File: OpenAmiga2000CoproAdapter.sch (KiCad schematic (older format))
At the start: 17 parts, among them CN1 A2000_COPRO_SLOT, P1 CONN_2, P10 CONN_1, P11 CONN_1, P12 CONN_1, P13 CONN_1, P14 CONN_1, P15 CONN_1, P2 CONN_2, P3 CONN_2, P4 CONN_2, P5 CONN_1, P6 CONN_1, P7 CONN_1, P8 CONN_1, P9 CONN_1, U1 68000D

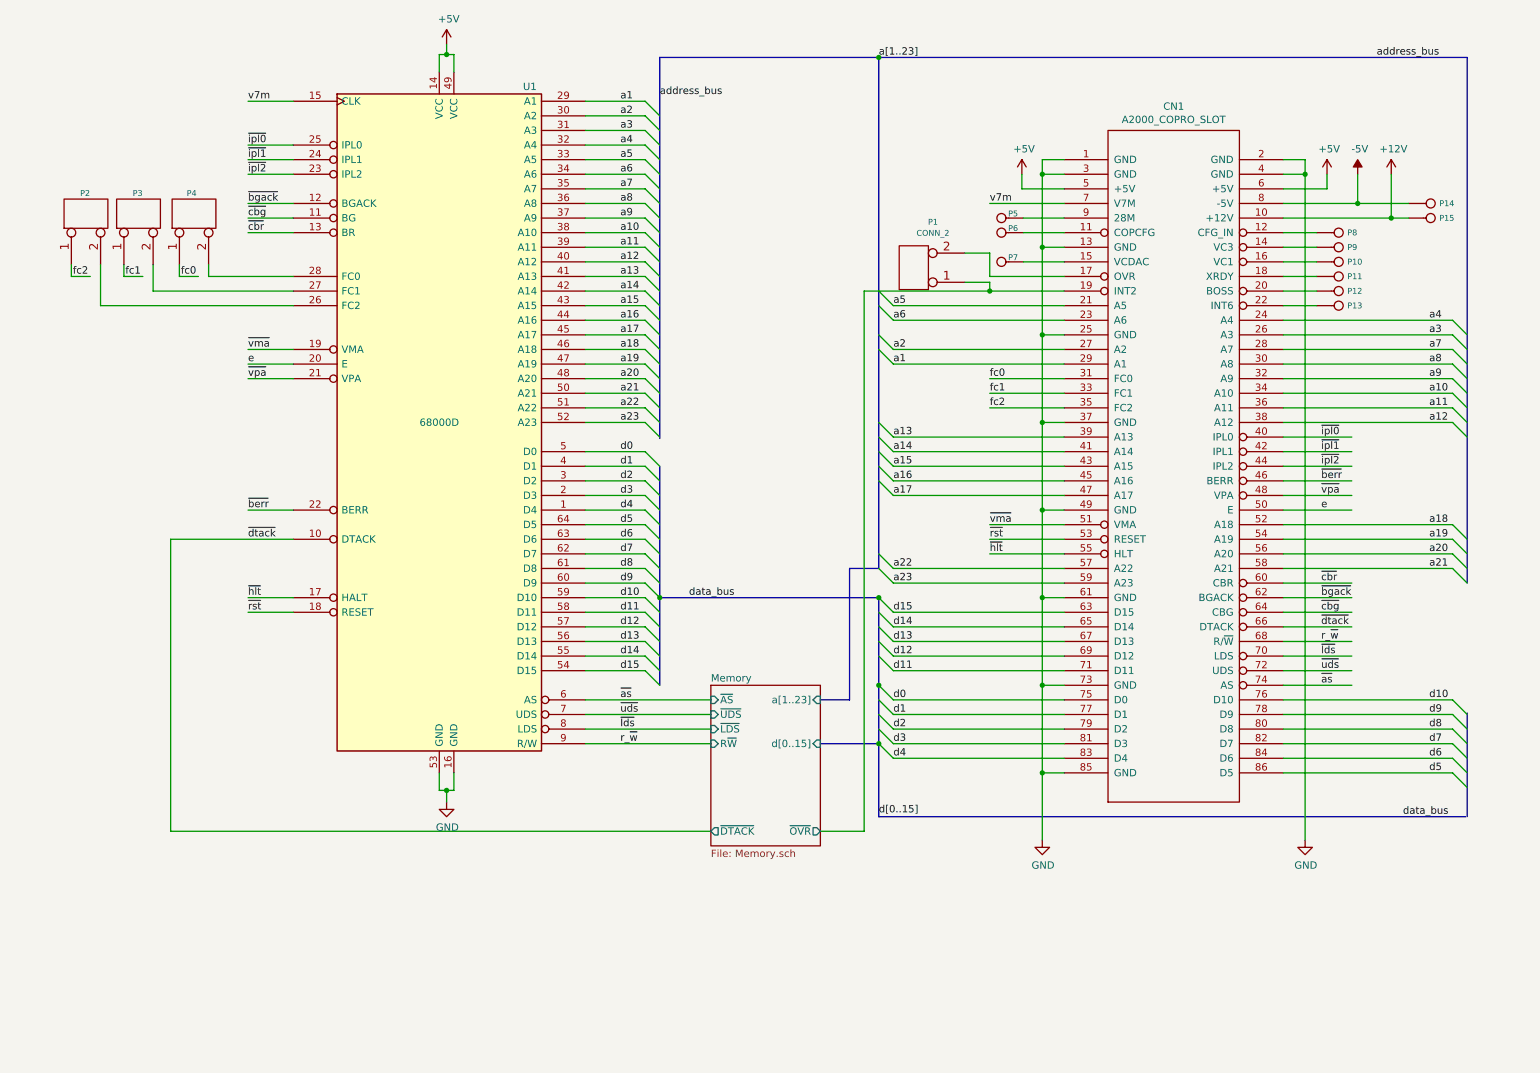
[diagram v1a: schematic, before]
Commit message: finish turbo section
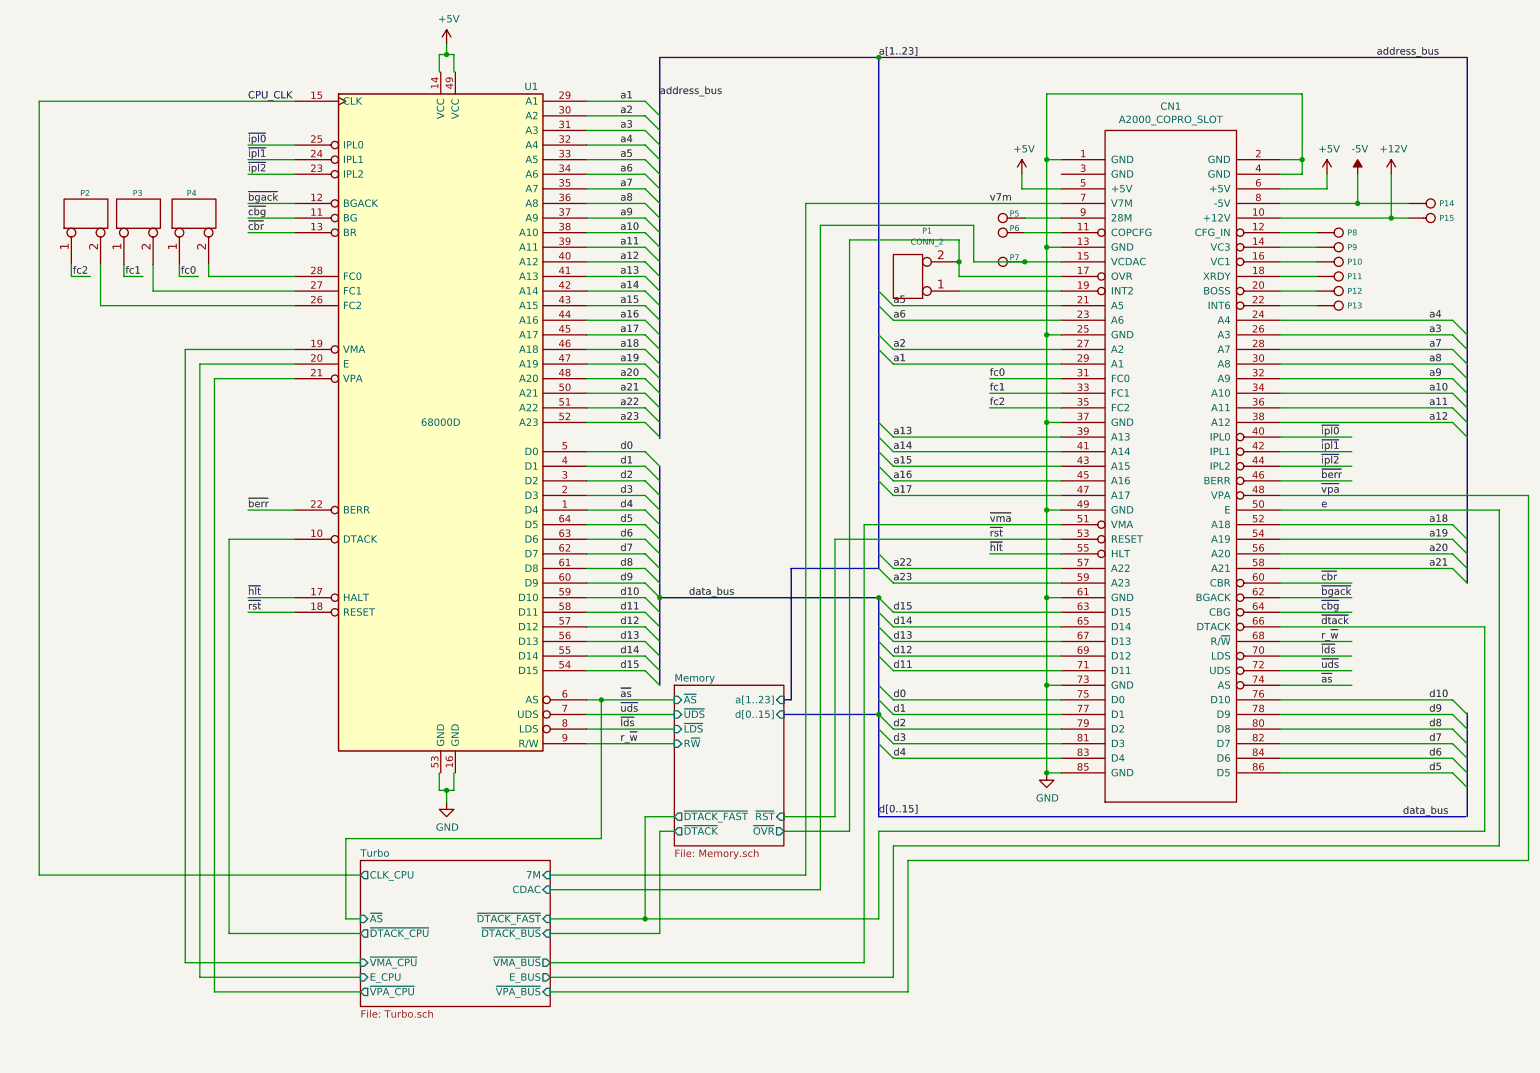
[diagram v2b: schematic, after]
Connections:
- net labels added: CPU_CLK
- wire segments 191 -> 230
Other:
- moved on the sheet: CN1, P1

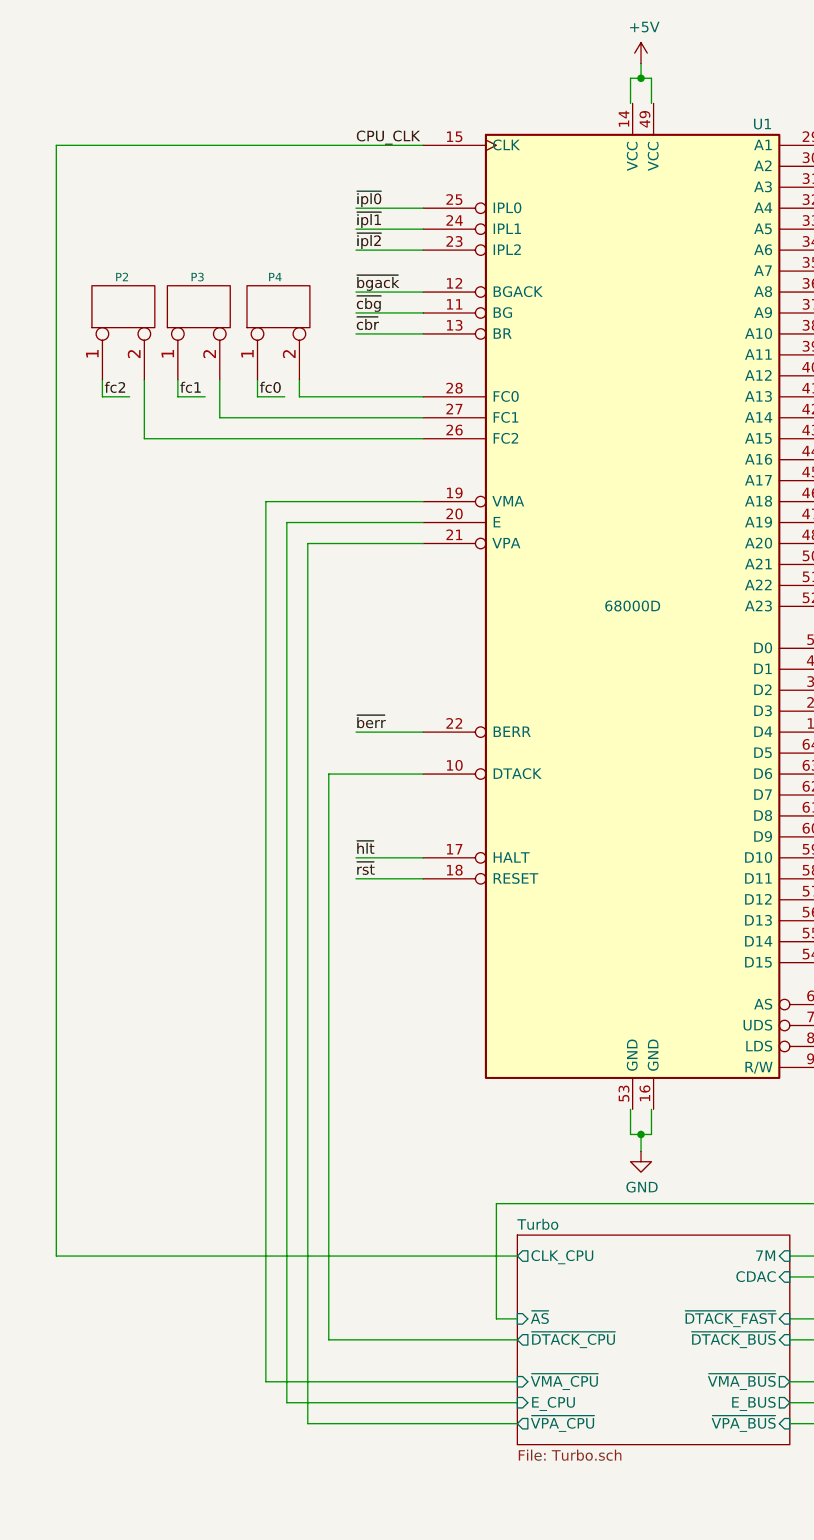
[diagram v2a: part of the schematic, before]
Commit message: add electrolytics
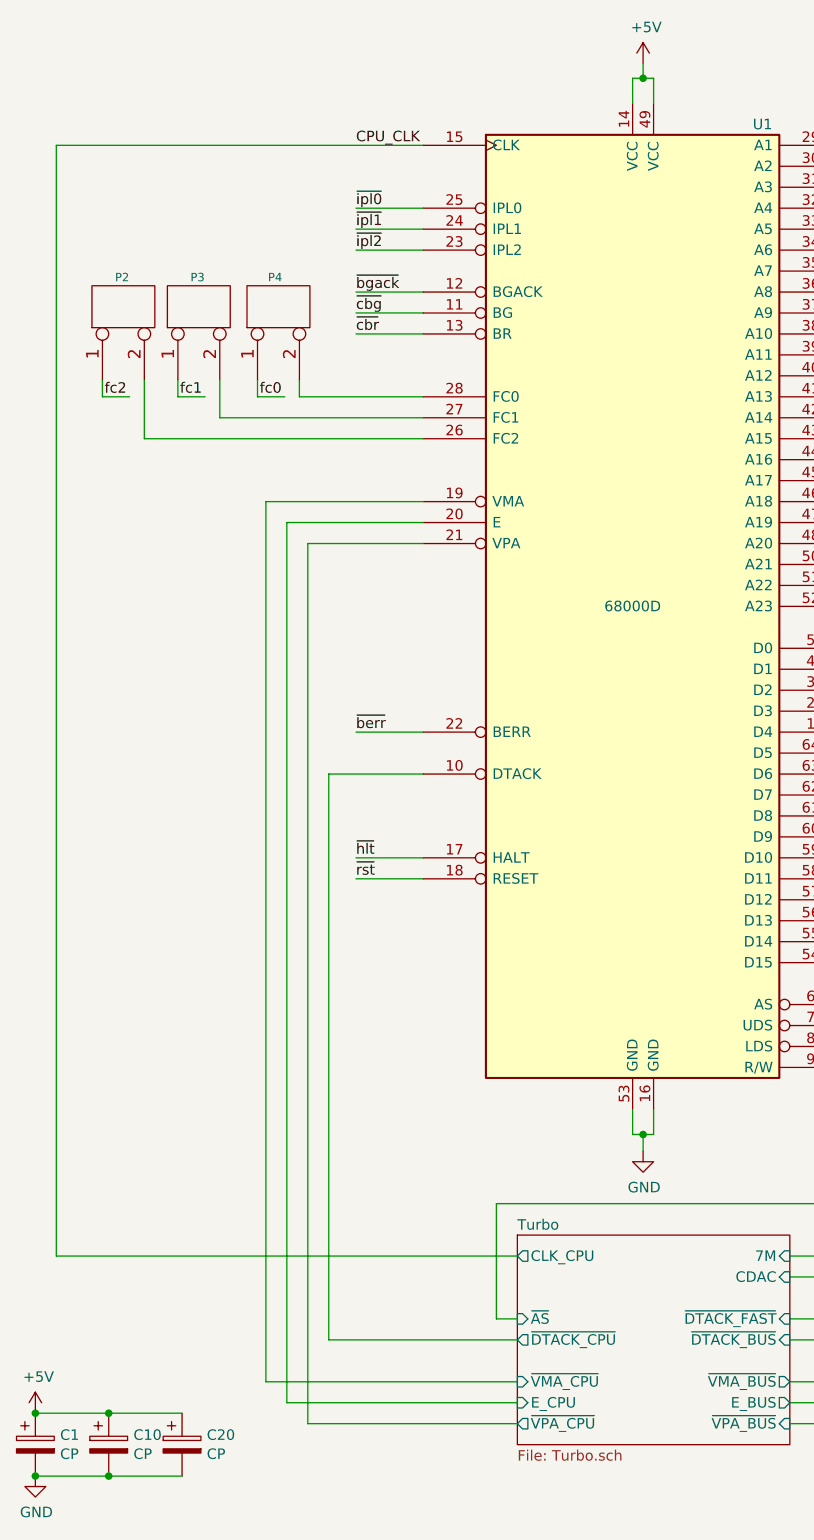
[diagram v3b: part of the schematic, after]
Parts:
- added C1, C10, C20: CP, symbol device:CP
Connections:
- wire segments 230 -> 234
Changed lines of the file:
@@
 a1
 Wire Wire Line
-	3540 5920 3590 5920
-Connection ~ 3540 5920
-Wire Wire Line
-	3540 6000 3540 5920
-$Comp
-L OpenAmiga2000CoproAdapter-rescue:GND-power #PWR08
-U 1 1 5BDCC79D
-P 3540 6000
-F 0 "#PWR08" H 3540 5750 50  0001 C CNN
-F 1 "GND" H 3545 5827 50  0000 C CNN
-F 2 "" H 3540 6000 50  0001 C CNN
-F 3 "" H 3540 6000 50  0001 C CNN
-	1    3540 6000
-	1    0    0    -1
-$EndComp
-Wire Wire Line
-	3590 5920 3590 5800
-Wire Wire Line
-	3490 5920 3540 5920
-Wire Wire Line
-	3490 5800 3490 5920
-Wire Wire Line
-	3540 880  3590 880
-Connection ~ 3540 880
-Wire Wire Line
-	3540 810  3540 880
+	3600 5920 3600 5800
+Wire Wire Line
+	3500 5800 3500 5920
+Wire Wire Line
+	3550 880  3600 880
+Connection ~ 3550 880
+Wire Wire Line
+	3550 810  3550 880
 $Comp
 L OpenAmiga2000CoproAdapter-rescue:+5V-power #PWR07
 U 1 1 5BDC734F
-P 3540 810
-F 0 "#PWR07" H 3540 660 50  0001 C CNN
-F 1 "+5V" H 3555 983 50  0000 C CNN
-F 2 "" H 3540 810 50  0001 C CNN
-F 3 "" H 3540 810 50  0001 C CNN
-	1    3540 810
-	1    0    0    -1
-$EndComp
-Wire Wire Line
-	3590 880  3590 1000
-Wire Wire Line
-	3490 880  3540 880
-Wire Wire Line
-	3490 1000 3490 880
+P 3550 810
+F 0 "#PWR07" H 3550 660 50  0001 C CNN
+F 1 "+5V" H 3565 983 50  0000 C CNN
+F 2 "" H 3550 810 50  0001 C CNN
+F 3 "" H 3550 810 50  0001 C CNN
+	1    3550 810
+	1    0    0    -1
+$EndComp
+Wire Wire Line
+	3600 880  3600 1000
+Wire Wire Line
+	3500 880  3550 880
+Wire Wire Line
+	3500 1000 3500 880
 Text Label 2180 1200 0    50   ~ 0
 CPU_CLK
@@
 Wire Wire Line
 	750  6500 2950 6500
+Wire Wire Line
+	3500 5920 3550 5920
+Wire Wire Line
+	3550 5920 3600 5920
+$Comp
+L OpenAmiga2000CoproAdapter-rescue:GND-power #PWR08
+U 1 1 5BDCC79D
+P 3550 6000
+F 0 "#PWR08" H 3550 5750 50  0001 C CNN
+F 1 "GND" H 3555 5827 50  0000 C CNN
+F 2 "" H 3550 6000 50  0001 C CNN
+F 3 "" H 3550 6000 50  0001 C CNN
+	1    3550 6000
+	1    0    0    -1
+$EndComp
+Wire Wire Line
+	3550 6000 3550 5920
+Connection ~ 3550 5920
+$Comp
+L device:CP C1
+U 1 1 60C785AA
+P 650 7400
+F 0 "C1" H 768 7446 50  0000 L CNN
+F 1 "CP" H 768 7355 50  0000 L CNN
+F 2 "" H 688 7250 50  0001 C CNN
+F 3 "~" H 650 7400 50  0001 C CNN
+	1    650  7400
+	1    0    0    -1
+$EndComp
+$Comp
+L device:CP C20
+U 1 1 60C796C0
+P 1350 7400
+F 0 "C20" H 1468 7446 50  0000 L CNN
+F 1 "CP" H 1468 7355 50  0000 L CNN
+F 2 "" H 1388 7250 50  0001 C CNN
+F 3 "~" H 1350 7400 50  0001 C CNN
+	1    1350 7400
+	1    0    0    -1
+$EndComp
+$Comp
+L device:CP C10
+U 1 1 60C79EDB
+P 1000 7400
+F 0 "C10" H 1118 7446 50  0000 L CNN
+F 1 "CP" H 1118 7355 50  0000 L CNN
+F 2 "" H 1038 7250 50  0001 C CNN
+F 3 "~" H 1000 7400 50  0001 C CNN
+	1    1000 7400
+	1    0    0    -1
+$EndComp
+Wire Wire Line
+	1350 7550 1000 7550
+Connection ~ 1000 7550
+Wire Wire Line
+	1000 7550 650  7550
+Wire Wire Line
+	650  7250 1000 7250
+Connection ~ 1000 7250
+Wire Wire Line
+	1000 7250 1350 7250
+$Comp
+L OpenAmiga2000CoproAdapter-rescue:GND-power #PWR0136
+U 1 1 60CDBCA7
+P 650 7550
+F 0 "#PWR0136" H 650 7300 50  0001 C CNN
+F 1 "GND" H 655 7377 50  0000 C CNN
+F 2 "" H 650 7550 50  0001 C CNN
+F 3 "" H 650 7550 50  0001 C CNN
+	1    650  7550
+	1    0    0    -1
+$EndComp
+Connection ~ 650  7550
+$Comp
+L OpenAmiga2000CoproAdapter-rescue:+5V-power #PWR0137
+U 1 1 60CDC65A
+P 650 7250
+F 0 "#PWR0137" H 650 7100 50  0001 C CNN
+F 1 "+5V" H 665 7423 50  0000 C CNN
+F 2 "" H 650 7250 50  0001 C CNN
+F 3 "" H 650 7250 50  0001 C CNN
+	1    650  7250
+	1    0    0    -1
+$EndComp
+Connection ~ 650  7250
 Wire Bus Line
 	6500 5400 6500 6100

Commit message: sheet metadata
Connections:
- wire segments 234 -> 236
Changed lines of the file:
@@
 encoding utf-8
 Sheet 1 3
-Title "OpenAmiga2000CoproAdapter"
+Title "LittleTurbo"
 Date "2019-02-14"
 Rev "2git"
-Comp "SukkoPera"
-Comment1 "Based on work by Kipper2K"
+Comp "Jan Hofmeier"
+Comment1 "Based on work by Kipper2K and SukkoPera"
 Comment2 "Licensed under CERN OHL v.1.2"
 Comment3 ""
@@
 Wire Wire Line
 	970  2400 1100 2400
-Text Label 980  2400 0    50   ~ 0
+Text Label 1100 2400 2    50   ~ 0
 fc2
-Text Label 1340 2400 0    50   ~ 0
+Text Label 1500 2400 2    50   ~ 0
 fc1
 Wire Wire Line
 	970  2320 970  2400
 Wire Wire Line
-	1330 2400 1460 2400
-Wire Wire Line
 	1330 2320 1330 2400
-Text Label 1720 2400 0    50   ~ 0
-fc0
-Wire Wire Line
-	1710 2400 1840 2400
 Wire Wire Line
 	1710 2320 1710 2400
@@
 Text Label 7260 4300 0    50   ~ 0
 ~hlt
-Text Label 9530 4500 0    50   ~ 0
-~cbr
-Text Label 9530 4600 0    50   ~ 0
-~bgack
-Text Label 9530 4700 0    50   ~ 0
-~cbg
-Text Label 9530 4800 0    50   ~ 0
-~dtack
-Text Label 9530 4900 0    50   ~ 0
+Text Label 9750 4900 2    50   ~ 0
 r_~w
-Text Label 9530 5000 0    50   ~ 0
+Text Label 9750 5000 2    50   ~ 0
 ~lds
-Text Label 9530 5100 0    50   ~ 0
+Text Label 9750 5100 2    50   ~ 0
 ~uds
-Text Label 9530 5200 0    50   ~ 0
+Text Label 9750 5200 2    50   ~ 0
 ~as
-Text Label 9530 3500 0    50   ~ 0
-~ipl0
-Text Label 9530 3600 0    50   ~ 0
-~ipl1
-Text Label 9530 3700 0    50   ~ 0
-~ipl2
-Text Label 9530 3800 0    50   ~ 0
-~berr
 Text Label 9530 3900 0    50   ~ 0
 ~vpa
@@
 	10650 6200 6500 6200
 Wire Wire Line
-	6500 6200 6500 6800
-Wire Wire Line
-	6500 6800 4900 6800
-Connection ~ 4900 6800
-Wire Wire Line
 	10750 4000 10750 6300
-Wire Wire Line
-	10750 6300 6600 6300
 Wire Wire Line
 	9400 1150 7650 1150
@@
 Connection ~ 7650 1600
 Wire Wire Line
-	7650 1600 7650 2200
+	7650 1600 7650 1700
 Wire Wire Line
 	7650 2200 7750 2200
@@
 	9250 3400 10430 3400
 Wire Wire Line
-	9250 3500 9740 3500
-Wire Wire Line
-	9250 3600 9740 3600
-Wire Wire Line
-	9250 3700 9740 3700
-Wire Wire Line
-	9250 3800 9740 3800
-Wire Wire Line
 	9250 4100 10430 4100
 Wire Wire Line
@@
 	9250 4400 10430 4400
 Wire Wire Line
-	9250 4500 9740 4500
-Wire Wire Line
-	9250 4600 9740 4600
-Wire Wire Line
-	9250 4700 9740 4700
-Wire Wire Line
 	9250 4800 10650 4800
-Wire Wire Line
-	9250 4900 9740 4900
-Wire Wire Line
-	9250 5000 9740 5000
-Wire Wire Line
-	9250 5100 9740 5100
-Wire Wire Line
-	9250 5200 9740 5200
 Wire Wire Line
 	9250 5300 10430 5300
@@
 Wire Wire Line
 	6700 7300 6700 6400
-Wire Wire Line
-	6700 6400 10950 6400
 Wire Wire Line
 	10950 6400 10950 3900
@@
 $EndComp
 Connection ~ 650  7250
+Wire Wire Line
+	5000 6900 6500 6900
+Connection ~ 5000 6900
+Wire Wire Line
+	6500 6200 6500 6900
+Wire Wire Line
+	10750 6300 6600 6300
+Wire Wire Line
+	6700 6400 10950 6400
+Text Label 1850 2400 2    50   ~ 0
+fc0
+Wire Wire Line
+	1330 2400 1500 2400
+Wire Wire Line
+	1710 2400 1850 2400
+Wire Wire Line
+	7750 1700 7650 1700
+Connection ~ 7650 1700
+Wire Wire Line
+	7650 1700 7650 2200
+Text Label 9650 3800 2    50   ~ 0
+~berr
+Text Label 9650 3700 2    50   ~ 0
+~ipl2
+Text Label 9650 3600 2    50   ~ 0
+~ipl1
+Text Label 9650 3500 2    50   ~ 0
+~ipl0
+Wire Wire Line
+	9250 3800 9650 3800
+Wire Wire Line
+	9250 3700 9650 3700
+Wire Wire Line
+	9250 3600 9650 3600
+Wire Wire Line
+	9250 3500 9650 3500
+Text Label 9750 4800 2    50   ~ 0
+~dtack
+Text Label 9750 4700 2    50   ~ 0
+~cbg
+Text Label 9750 4600 2    50   ~ 0
+~bgack
+Text Label 9750 4500 2    50   ~ 0
+~cbr
+Wire Wire Line
+	9250 4500 9750 4500
+Wire Wire Line
+	9250 4600 9750 4600
+Wire Wire Line
+	9250 4700 9750 4700
+Wire Wire Line
+	9250 4900 9750 4900
+Wire Wire Line
+	9250 5000 9750 5000
+Wire Wire Line
+	9250 5100 9750 5100
+Wire Wire Line
+	9250 5200 9750 5200
 Wire Bus Line
 	6500 5400 6500 6100

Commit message: assign footprints
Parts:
- C1, C10, C20: value CP -> 47uF; footprint (none) -> Capacitor_THT:CP_Radial_D5.0mm_P2.50mm
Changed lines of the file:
@@
 P 650 7400
 F 0 "C1" H 768 7446 50  0000 L CNN
-F 1 "CP" H 768 7355 50  0000 L CNN
-F 2 "" H 688 7250 50  0001 C CNN
+F 1 "47uF" H 700 7300 50  0000 L CNN
+F 2 "Capacitor_THT:CP_Radial_D5.0mm_P2.50mm" H 688 7250 50  0001 C CNN
 F 3 "~" H 650 7400 50  0001 C CNN
 	1    650  7400
@@
 P 1350 7400
 F 0 "C20" H 1468 7446 50  0000 L CNN
-F 1 "CP" H 1468 7355 50  0000 L CNN
-F 2 "" H 1388 7250 50  0001 C CNN
+F 1 "47uF" H 1400 7300 50  0000 L CNN
+F 2 "Capacitor_THT:CP_Radial_D5.0mm_P2.50mm" H 1388 7250 50  0001 C CNN
 F 3 "~" H 1350 7400 50  0001 C CNN
 	1    1350 7400
@@
 P 1000 7400
 F 0 "C10" H 1118 7446 50  0000 L CNN
-F 1 "CP" H 1118 7355 50  0000 L CNN
-F 2 "" H 1038 7250 50  0001 C CNN
+F 1 "47uF" H 1050 7300 50  0000 L CNN
+F 2 "Capacitor_THT:CP_Radial_D5.0mm_P2.50mm" H 1038 7250 50  0001 C CNN
 F 3 "~" H 1000 7400 50  0001 C CNN
 	1    1000 7400

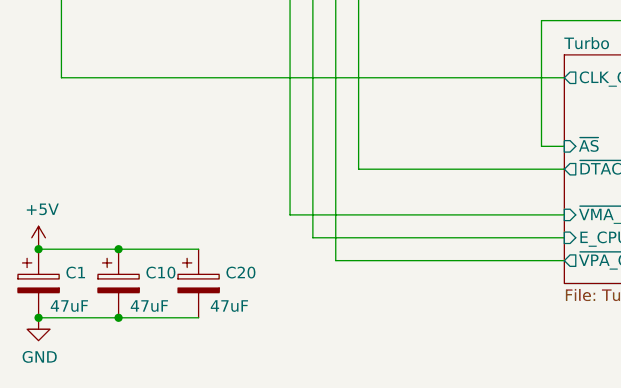
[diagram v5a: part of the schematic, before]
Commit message: routed upper  byte
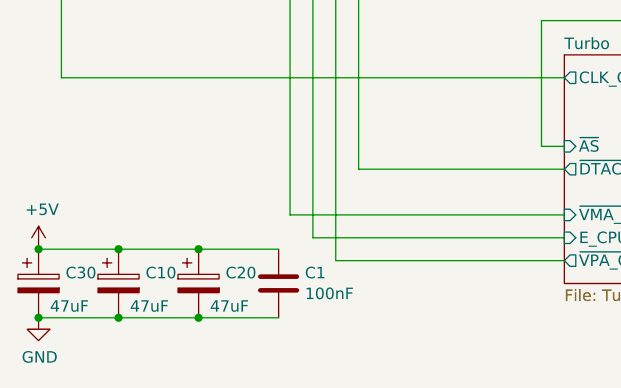
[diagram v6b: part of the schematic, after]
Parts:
- added C1: 100nF, Capacitor_THT:C_Disc_D7.0mm_W2.5mm_P5.00mm, symbol device:C
- renumbered C1 to C30
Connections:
- net +5V: now also C1.1
- net GND: now also C1.2
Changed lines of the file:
@@
 Connection ~ 3550 5920
 $Comp
-L device:CP C1
+L device:CP C30
 U 1 1 60C785AA
 P 650 7400
-F 0 "C1" H 768 7446 50  0000 L CNN
+F 0 "C30" H 768 7446 50  0000 L CNN
 F 1 "47uF" H 700 7300 50  0000 L CNN
 F 2 "Capacitor_THT:CP_Radial_D5.0mm_P2.50mm" H 688 7250 50  0001 C CNN
@@
 Wire Wire Line
 	9250 5200 9750 5200
+$Comp
+L device:C C1
+U 1 1 601C897C
+P 1700 7400
+F 0 "C1" H 1815 7446 50  0000 L CNN
+F 1 "100nF" H 1815 7355 50  0000 L CNN
+F 2 "Capacitor_THT:C_Disc_D7.0mm_W2.5mm_P5.00mm" H 1738 7250 50  0001 C CNN
+F 3 "~" H 1700 7400 50  0001 C CNN
+	1    1700 7400
+	1    0    0    -1
+$EndComp
+Wire Wire Line
+	1700 7250 1350 7250
+Connection ~ 1350 7250
+Wire Wire Line
+	1350 7550 1700 7550
 Wire Bus Line
 	6500 5400 6500 6100
@@
 Wire Bus Line
 	5000 900  5000 3510
+Connection ~ 1350 7550
 $EndSCHEMATC
